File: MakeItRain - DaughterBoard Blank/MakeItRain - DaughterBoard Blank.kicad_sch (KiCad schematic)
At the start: 1 part, among them J1 Conn_02x15_Odd_Even

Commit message: updating some routes, updating the already done daughterboard and updating the blank layout for both.
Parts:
- removed J1: Conn_02x15_Odd_Even, Connector_PinHeader_2.54mm:PinHeader_2x15_P2.54mm_Vertical, symbol Connector_Generic:Conn_02x15_Odd_Even
- added J1: Conn_02x14_Odd_Even, Connector_PinHeader_2.54mm:PinHeader_2x14_P2.54mm_Vertical, symbol Connector_Generic:Conn_02x14_Odd_Even
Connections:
- net +3V3: now also J1.11 (Pin_11), J1.13 (Pin_13), J1.15 (Pin_15), J1.17 (Pin_17)
- net +VDC: now also J1.1 (Pin_1), J1.3 (Pin_3), J1.5 (Pin_5), J1.7 (Pin_7), J1.9 (Pin_9)
- net D18: now also J1.20 (Pin_20)
- net D19: now also J1.18 (Pin_18)
- net D23: now also J1.16 (Pin_16)
- net GND: now also J1.19 (Pin_19), J1.21 (Pin_21), J1.23 (Pin_23), J1.25 (Pin_25), J1.27 (Pin_27)
- net RX: now also J1.28 (Pin_28)
- net TX: now also J1.26 (Pin_26)
- new net D16: J1.24 (Pin_24)
- new net D17: J1.22 (Pin_22)
- new net D26: J1.14 (Pin_14)
- new net SCL: J1.2 (Pin_2)
- new net SDA: J1.4 (Pin_4)
- new net Z5: J1.12 (Pin_12)
- new net Z6: J1.10 (Pin_10)
- new net Z7: J1.8 (Pin_8)
- new net Z8: J1.6 (Pin_6)

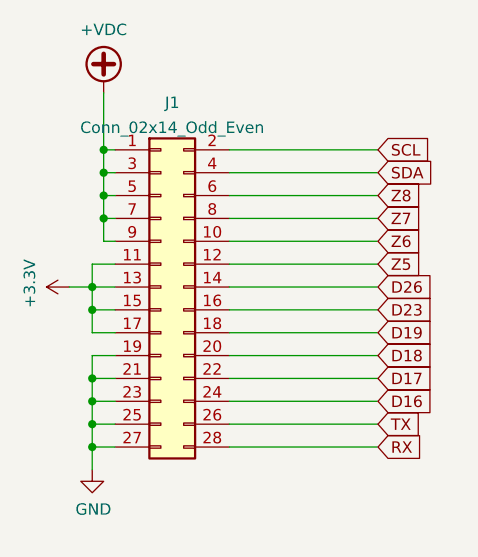
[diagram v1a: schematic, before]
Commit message: MakeItRain * Main Board Fixed Routing. * replaced Opamp with the part that i can get as the old one is EOL * generated all the fab files i need. * updated the daughter plug witht eh i2c ttl flip * fixed I2C issues * DRC'ed the board
MakeItRain - DaughterBoard - Zone Expansion
* updated the daughter plug witht eh i2c ttl flip
* fixed some of the routings
* generated new fab files
* DRC'ed the board
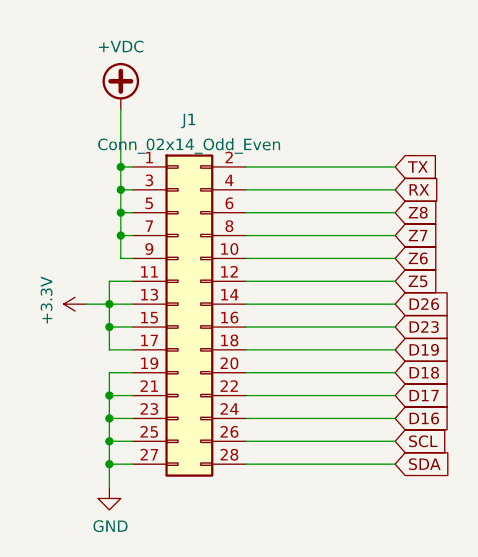
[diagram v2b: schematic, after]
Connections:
- net RX: now also J1.4 (Pin_4); no longer J1.28 (Pin_28)
- net SCL: now also J1.26 (Pin_26); no longer J1.2 (Pin_2)
- net SDA: now also J1.28 (Pin_28); no longer J1.4 (Pin_4)
- net TX: now also J1.2 (Pin_2); no longer J1.26 (Pin_26)
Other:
- moved on the sheet: J1
